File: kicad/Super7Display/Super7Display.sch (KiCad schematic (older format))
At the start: 8 parts, among them P1 CONN_01X13, P2 CONN_01X09

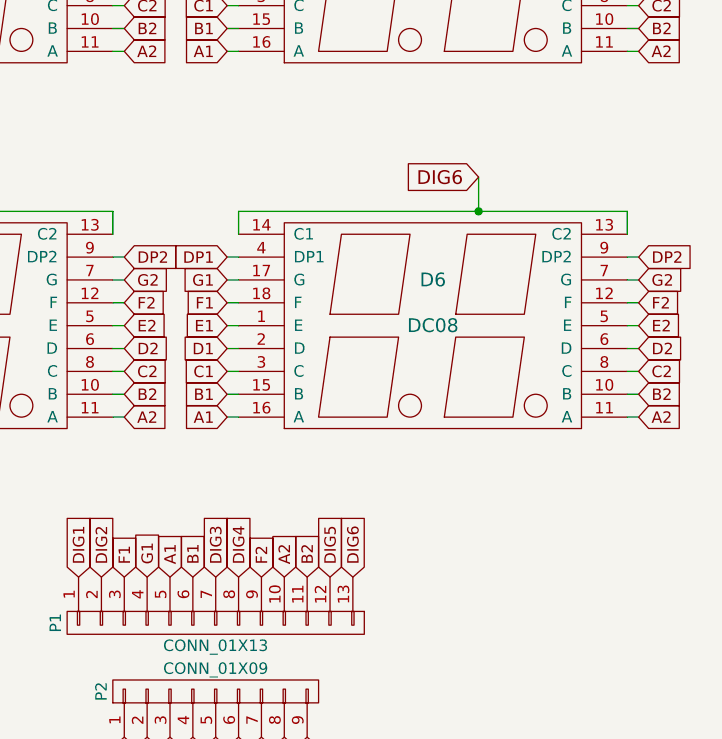
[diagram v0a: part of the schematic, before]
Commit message: Remove DIG6 from schematic
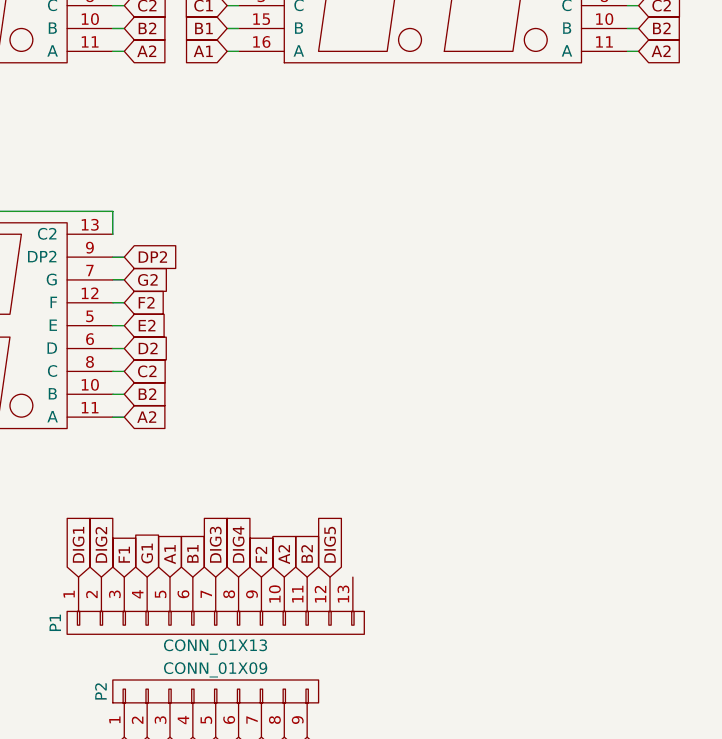
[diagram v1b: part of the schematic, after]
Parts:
- removed D6: DC08, footprints:DC08, symbol DC08
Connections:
- net DIG6: no longer names the net of P1.13 (P13)
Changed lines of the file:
@@
 Text GLabel 2650 4600 2    50   Input ~ 0
 DP2
-$Comp
-L DC08 D6
-U 1 1 585D8436
-P 4000 4900
-F 0 "D6" H 4000 5100 60  0000 C CNN
-F 1 "DC08" H 4000 4900 60  0000 C CNN
-F 2 "footprints:DC08" H 4400 4600 60  0001 C CNN
-F 3 "" H 4400 4600 60  0000 C CNN
-	1    4000 4900
-	1    0    0    -1
-$EndComp
-Text GLabel 3100 5300 0    50   Input ~ 0
-A1
-Text GLabel 3100 5200 0    50   Input ~ 0
-B1
-Text GLabel 3100 5100 0    50   Input ~ 0
-C1
-Text GLabel 3100 5000 0    50   Input ~ 0
-D1
-Text GLabel 3100 4900 0    50   Input ~ 0
-E1
-Text GLabel 3100 4800 0    50   Input ~ 0
-F1
-Text GLabel 3100 4700 0    50   Input ~ 0
-G1
-Text GLabel 3100 4600 0    50   Input ~ 0
-DP1
-Text GLabel 4900 5300 2    50   Input ~ 0
-A2
-Text GLabel 4900 5200 2    50   Input ~ 0
-B2
-Text GLabel 4900 5100 2    50   Input ~ 0
-C2
-Text GLabel 4900 5000 2    50   Input ~ 0
-D2
-Text GLabel 4900 4900 2    50   Input ~ 0
-E2
-Text GLabel 4900 4800 2    50   Input ~ 0
-F2
-Text GLabel 4900 4700 2    50   Input ~ 0
-G2
-Text GLabel 4900 4600 2    50   Input ~ 0
-DP2
 Wire Wire Line
 	850  1400 900  1400
@@
 	2600 5300 2650 5300
 Wire Wire Line
-	3100 4600 3150 4600
-Wire Wire Line
-	3150 4700 3100 4700
-Wire Wire Line
-	3100 4800 3150 4800
-Wire Wire Line
-	3150 4900 3100 4900
-Wire Wire Line
-	3100 5000 3150 5000
-Wire Wire Line
-	3150 5100 3100 5100
-Wire Wire Line
-	3100 5200 3150 5200
-Wire Wire Line
-	3150 5300 3100 5300
-Wire Wire Line
-	4900 4600 4850 4600
-Wire Wire Line
-	4850 4700 4900 4700
-Wire Wire Line
-	4900 4800 4850 4800
-Wire Wire Line
-	4850 4900 4900 4900
-Wire Wire Line
-	4900 5000 4850 5000
-Wire Wire Line
-	4850 5100 4900 5100
-Wire Wire Line
-	4900 5200 4850 5200
-Wire Wire Line
-	4850 5300 4900 5300
-Wire Wire Line
 	1550 4400 1550 4250
 Wire Wire Line
@@
 	2600 4400 2600 4500
 Connection ~ 1550 4400
-Wire Wire Line
-	4200 4250 4200 4400
-Wire Wire Line
-	3150 4400 4850 4400
-Wire Wire Line
-	4850 4400 4850 4500
-Wire Wire Line
-	3150 4400 3150 4500
-Connection ~ 4200 4400
 Text GLabel 1550 1050 0    60   Input ~ 0
 DIG1
@@
 Text GLabel 1550 4250 0    60   Input ~ 0
 DIG5
-Text GLabel 4200 4250 0    60   Input ~ 0
-DIG6
 Text GLabel 3350 6000 1    50   Input ~ 0
 A2
@@
 Text GLabel 3550 6000 1    50   Input ~ 0
 DIG5
-Text GLabel 3650 6000 1    50   Input ~ 0
-DIG6
+$Comp
+L CONN_01X09 P2
+U 1 1 5867A860
+P 3050 6500
+F 0 "P2" H 3050 7000 50  0000 C CNN
+F 1 "CONN_01X09" V 3150 6500 50  0000 C CNN
+F 2 "Socket_Strips:Socket_Strip_Straight_1x09" H 3050 6500 50  0001 C CNN
+F 3 "" H 3050 6500 50  0000 C CNN
+	1    3050 6500
+	0    -1   -1   0
+$EndComp
 $Comp
 L CONN_01X13 P1
@@
 	0    -1   1    0
 $EndComp
-$Comp
-L CONN_01X09 P2
-U 1 1 5867A860
-P 3050 6500
-F 0 "P2" H 3050 7000 50  0000 C CNN
-F 1 "CONN_01X09" V 3150 6500 50  0000 C CNN
-F 2 "Socket_Strips:Socket_Strip_Straight_1x09" H 3050 6500 50  0001 C CNN
-F 3 "" H 3050 6500 50  0000 C CNN
-	1    3050 6500
-	0    -1   -1   0
-$EndComp
 $EndSCHEMATC
